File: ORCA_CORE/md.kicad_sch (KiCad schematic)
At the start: 23 parts, among them J13 md_out, J15 limit_sw_upper, J20 limit_sw_under, J22 Vin_motor, U10 TLP293, U4 AM2837, U6 TLP293, U8 AZ1117-3.3

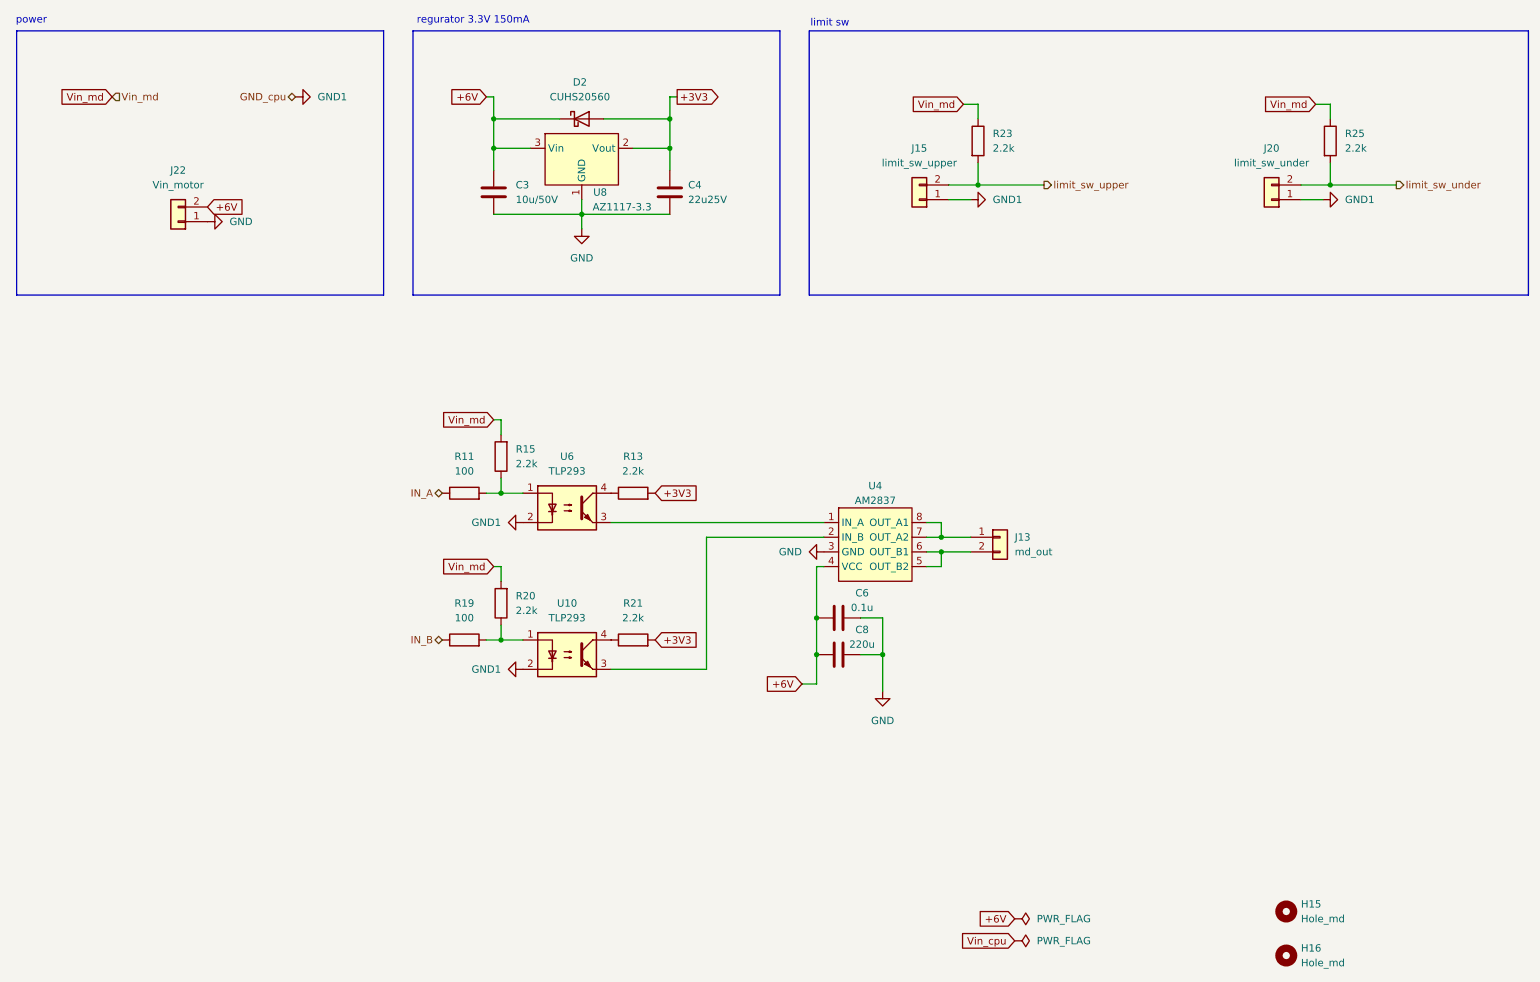
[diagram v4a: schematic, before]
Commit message: complete almost all wires. add mouse coms sensor
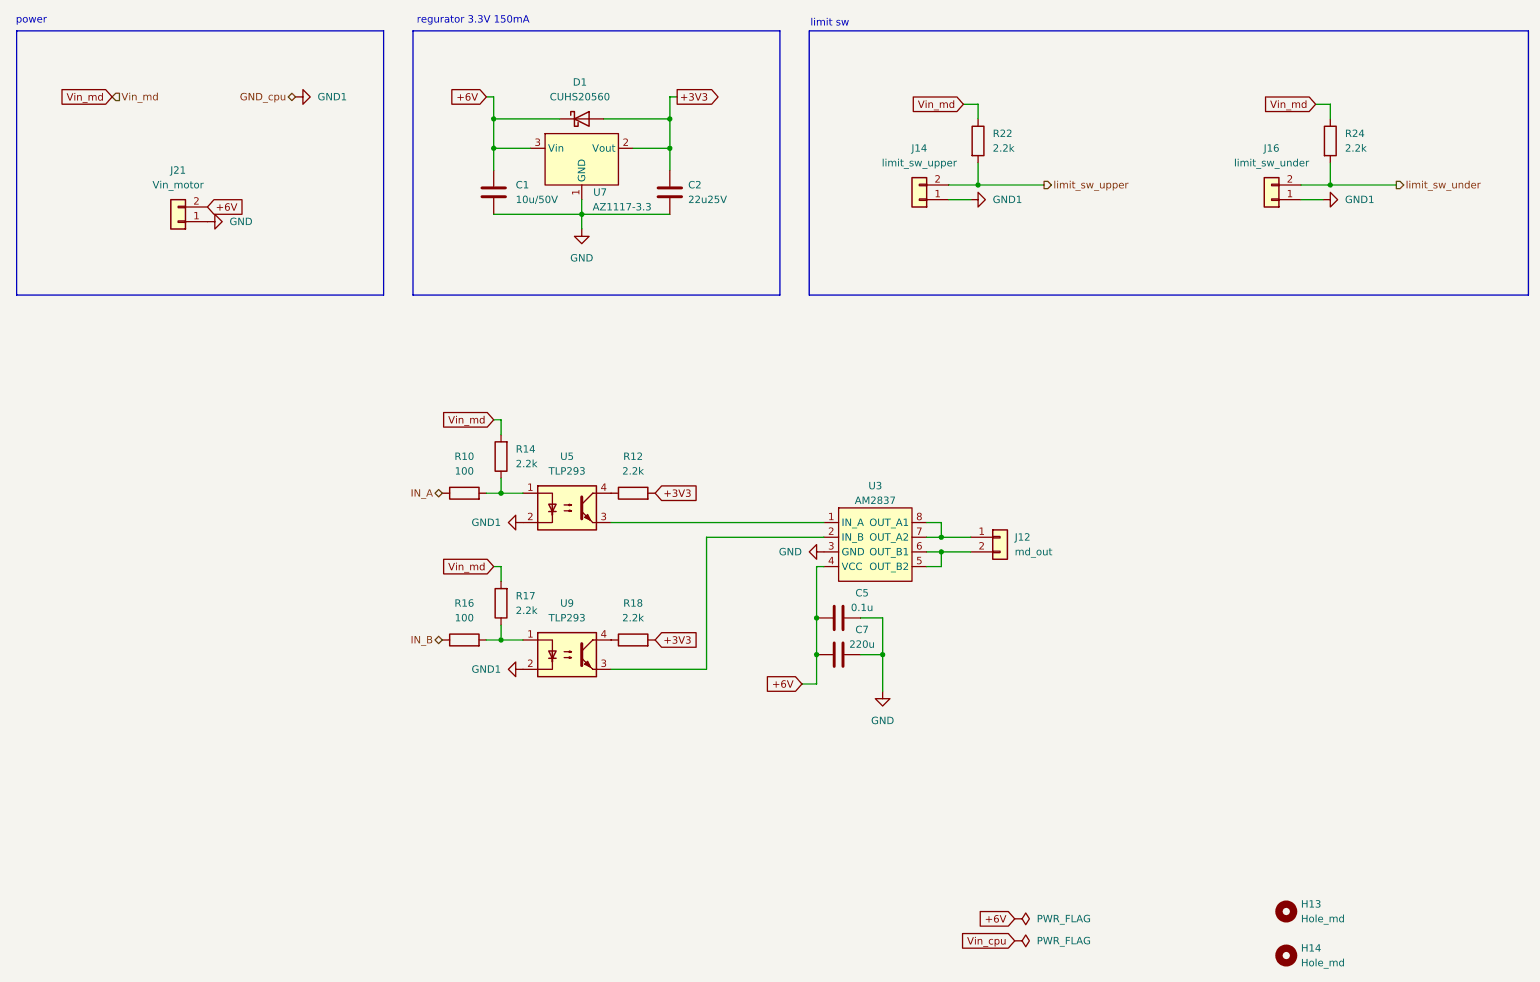
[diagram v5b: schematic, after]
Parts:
- renumbered C3 to C1, C4 to C2, C6 to C5, C8 to C7, D2 to D1, H15 to H13, H16 to H14, J13 to J12, J15 to J14, J20 to J16, J22 to J21, R11 to R10, R13 to R12, R15 to R14, R19 to R16, R20 to R17, R21 to R18, R23 to R22, R25 to R24, U4 to U3, U6 to U5, U8 to U7, U10 to U9
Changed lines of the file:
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@@
 (kicad_sch
-	(version 20231120)
+	(version 20250114)
 	(generator "eeschema")
-	(generator_version "8.0")
+	(generator_version "9.0")
 	(paper "A4")
+	(rectangle
+		(start 154.94 17.78)
+		(end 279.4 63.5)
+		(stroke
+			(width 0)
+			(type default)
+		)
+		(fill
+			(type none)
+		)
+	)
+	(rectangle
+		(start 17.78 17.78)
+		(end 81.28 63.5)
+		(stroke
+			(width 0)
+			(type default)
+		)
+		(fill
+			(type none)
+		)
+	)
+	(rectangle
+		(start 86.36 17.78)
+		(end 149.86 63.5)
+		(stroke
+			(width 0)
+			(type default)
+		)
+		(fill
+			(type none)
+		)
+	)
+	(text "regurator 3.3V 150mA"
+		(exclude_from_sim no)
+		(at 96.774 16.002 0)
+		(effects
+			(font
+				(size 1.27 1.27)
+			)
+		)
+	)
+	(text "power"
+		(exclude_from_sim no)
+		(at 20.32 16.002 0)
+		(effects
+			(font
+				(size 1.27 1.27)
+			)
+		)
+	)
+	(text "limit sw"
+		(exclude_from_sim no)
+		(at 158.496 16.51 0)
+		(effects
+			(font
+				(size 1.27 1.27)
+			)
+		)
+	)
 	(junction
 		(at 115.57 49.53)
@@
 		)
 	)
-	(rectangle
-		(start 154.94 17.78)
-		(end 279.4 63.5)
-		(stroke
-			(width 0)
-			(type default)
-		)
-		(fill
-			(type none)
-		)
-	)
-	(rectangle
-		(start 17.78 17.78)
-		(end 81.28 63.5)
-		(stroke
-			(width 0)
-			(type default)
-		)
-		(fill
-			(type none)
-		)
-	)
-	(rectangle
-		(start 86.36 17.78)
-		(end 149.86 63.5)
-		(stroke
-			(width 0)
-			(type default)
-		)
-		(fill
-			(type none)
-		)
-	)
-	(text "regurator 3.3V 150mA"
-		(exclude_from_sim no)
-		(at 96.774 16.002 0)
-		(effects
-			(font
-				(size 1.27 1.27)
-			)
-		)
-	)
-	(text "power"
-		(exclude_from_sim no)
-		(at 20.32 16.002 0)
-		(effects
-			(font
-				(size 1.27 1.27)
-			)
-		)
-	)
-	(text "limit sw"
-		(exclude_from_sim no)
-		(at 158.496 16.51 0)
-		(effects
-			(font
-				(size 1.27 1.27)
-			)
-		)
-	)
 	(global_label "+6V"
 		(shape input)
@@
 		(shape output)
 		(at 195.58 44.45 0)
-		(fields_autoplaced yes)
 		(effects
 			(font
@@
 		(shape input)
 		(at 34.29 29.21 0)
-		(fields_autoplaced yes)
 		(effects
 			(font
@@
 		(shape bidirectional)
 		(at 66.04 29.21 180)
-		(fields_autoplaced yes)
 		(effects
 			(font
@@
 		(shape output)
 		(at 256.54 44.45 0)
-		(fields_autoplaced yes)
 		(effects
 			(font
@@
 		(shape bidirectional)
 		(at 91.44 123.19 180)
-		(fields_autoplaced yes)
 		(effects
 			(font
@@
 		(shape bidirectional)
 		(at 91.44 97.79 180)
-		(fields_autoplaced yes)
 		(effects
 			(font
@@
 		(dnp no)
 		(fields_autoplaced yes)
-		(property "Reference" "#PWR041"
+		(property "Reference" "#PWR040"
 			(at 151.13 107.95 0)
 			(effects
@@
 		(dnp no)
 		(fields_autoplaced yes)
-		(property "Reference" "C3"
+		(property "Reference" "C1"
 			(at 104.14 44.45 0)
 			(effects
@@
 		(dnp no)
 		(fields_autoplaced yes)
-		(property "Reference" "R15"
+		(property "Reference" "R14"
 			(at 104.14 90.1699 0)
 			(effects
@@
 		(dnp no)
 		(fields_autoplaced yes)
-		(property "Reference" "#PWR043"
+		(property "Reference" "#PWR042"
 			(at 99.06 128.27 0)
 			(effects
@@
 		(dnp no)
 		(fields_autoplaced yes)
-		(property "Reference" "R23"
+		(property "Reference" "R22"
 			(at 186.69 35.5599 0)
 			(effects
@@
 		(on_board yes)
 		(dnp no)
-		(property "Reference" "U8"
+		(property "Reference" "U7"
 			(at 118.745 45.72 0)
 			(effects
@@
 		(dnp no)
 		(fields_autoplaced yes)
-		(property "Reference" "R19"
+		(property "Reference" "R16"
 			(at 95.25 116.84 90)
 			(effects
@@
 		(dnp no)
 		(fields_autoplaced yes)
-		(property "Reference" "#PWR047"
+		(property "Reference" "#PWR046"
 			(at 189.23 46.99 0)
 			(effects
@@
 		(dnp no)
 		(fields_autoplaced yes)
-		(property "Reference" "J13"
+		(property "Reference" "J12"
 			(at 190.5 105.4099 0)
 			(effects
@@
 		(dnp no)
 		(fields_autoplaced yes)
-		(property "Reference" "#PWR049"
+		(property "Reference" "#PWR048"
 			(at 250.19 46.99 0)
 			(effects
@@
 		(dnp no)
 		(fields_autoplaced yes)
-		(property "Reference" "#PWR035"
+		(property "Reference" "#PWR026"
 			(at 72.39 29.21 0)
 			(effects
@@
 		(dnp no)
 		(fields_autoplaced yes)
-		(property "Reference" "#FLG03"
+		(property "Reference" "#FLG02"
 			(at 192.405 171.45 0)
 			(effects
@@
 		(dnp no)
 		(fields_autoplaced yes)
-		(property "Reference" "J20"
+		(property "Reference" "J16"
 			(at 234.95 38.1 0)
 			(effects
@@
 		(dnp no)
 		(fields_autoplaced yes)
-		(property "Reference" "#PWR039"
+		(property "Reference" "#PWR038"
 			(at 99.06 102.87 0)
 			(effects
@@
 		(dnp no)
 		(fields_autoplaced yes)
-		(property "Reference" "H15"
+		(property "Reference" "H13"
 			(at 240.03 168.9099 0)
 			(effects
@@
 		(on_board yes)
 		(dnp no)
-		(property "Reference" "C6"
+		(property "Reference" "C5"
 			(at 164.084 115.062 90)
 			(effects
@@
 		(dnp no)
 		(fields_autoplaced yes)
-		(property "Reference" "J15"
+		(property "Reference" "J14"
 			(at 173.99 38.1 0)
 			(effects
@@
 		(on_board yes)
 		(dnp no)
-		(property "Reference" "C8"
+		(property "Reference" "C7"
 			(at 164.084 121.412 90)
 			(effects
@@
 		(dnp no)
 		(fields_autoplaced yes)
-		(property "Reference" "#PWR051"
+		(property "Reference" "#PWR050"
 			(at 167.64 138.43 0)
 			(effects
@@
 		(dnp no)
 		(fields_autoplaced yes)
-		(property "Reference" "R25"
+		(property "Reference" "R24"
 			(at 247.65 35.5599 0)
 			(effects
@@
 		(dnp no)
 		(fields_autoplaced yes)
-		(property "Reference" "R11"
+		(property "Reference" "R10"
 			(at 95.25 91.44 90)
 			(effects
@@
 		(dnp no)
 		(fields_autoplaced yes)
-		(property "Reference" "H16"
+		(property "Reference" "H14"
 			(at 240.03 176.5299 0)
 			(effects
@@
 		(dnp no)
 		(fields_autoplaced yes)
-		(property "Reference" "D2"
+		(property "Reference" "D1"
 			(at 115.2525 26.67 0)
 			(effects
@@
 		(dnp no)
 		(fields_autoplaced yes)
-		(property "Reference" "J22"
+		(property "Reference" "J21"
 			(at 45.72 41.91 0)
 			(effects
@@
 		(dnp no)
 		(fields_autoplaced yes)
-		(property "Reference" "C4"
+		(property "Reference" "C2"
 			(at 133.985 44.45 0)
 			(effects
@@
 		(dnp no)
 		(fields_autoplaced yes)
-		(property "Reference" "R20"
+		(property "Reference" "R17"
 			(at 104.14 115.5699 0)
 			(effects
@@
 		(dnp no)
 		(fields_autoplaced yes)
-		(property "Reference" "U4"
+		(property "Reference" "U3"
 			(at 166.37 96.52 0)
 			(effects
@@
 		(dnp no)
 		(fields_autoplaced yes)
-		(property "Reference" "#PWR045"
+		(property "Reference" "#PWR044"
 			(at 115.57 58.42 0)
 			(effects
@@
 		(dnp no)
 		(fields_autoplaced yes)
-		(property "Reference" "#PWR053"
+		(property "Reference" "#PWR052"
 			(at 57.15 50.8 0)
 			(effects
@@
 		(dnp no)
 		(fields_autoplaced yes)
-		(property "Reference" "U10"
+		(property "Reference" "U9"
 			(at 113.03 116.84 0)
 			(effects
@@
 		(dnp no)
 		(fields_autoplaced yes)
-		(property "Reference" "#FLG05"
+		(property "Reference" "#FLG04"
 			(at 192.405 175.26 0)
 			(effects
@@
 		(dnp no)
 		(fields_autoplaced yes)
-		(property "Reference" "R21"
+		(property "Reference" "R18"
 			(at 124.46 116.84 90)
 			(effects
@@
 		(dnp no)
 		(fields_autoplaced yes)
-		(property "Reference" "U6"
+		(property "Reference" "U5"
 			(at 113.03 91.44 0)
 			(effects
@@
 		(dnp no)
 		(fields_autoplaced yes)
-		(property "Reference" "R13"
+		(property "Reference" "R12"
 			(at 124.46 91.44 90)
 			(effects

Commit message: end wiring
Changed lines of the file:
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@@
 		)
 	)
-	(hierarchical_label "GND_cpu"
+	(hierarchical_label "GND_md"
 		(shape bidirectional)
 		(at 66.04 29.21 180)
